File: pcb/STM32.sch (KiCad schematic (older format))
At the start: 30 parts, among them J1 Conn_02x07_Odd_Even, X1 ABM8G

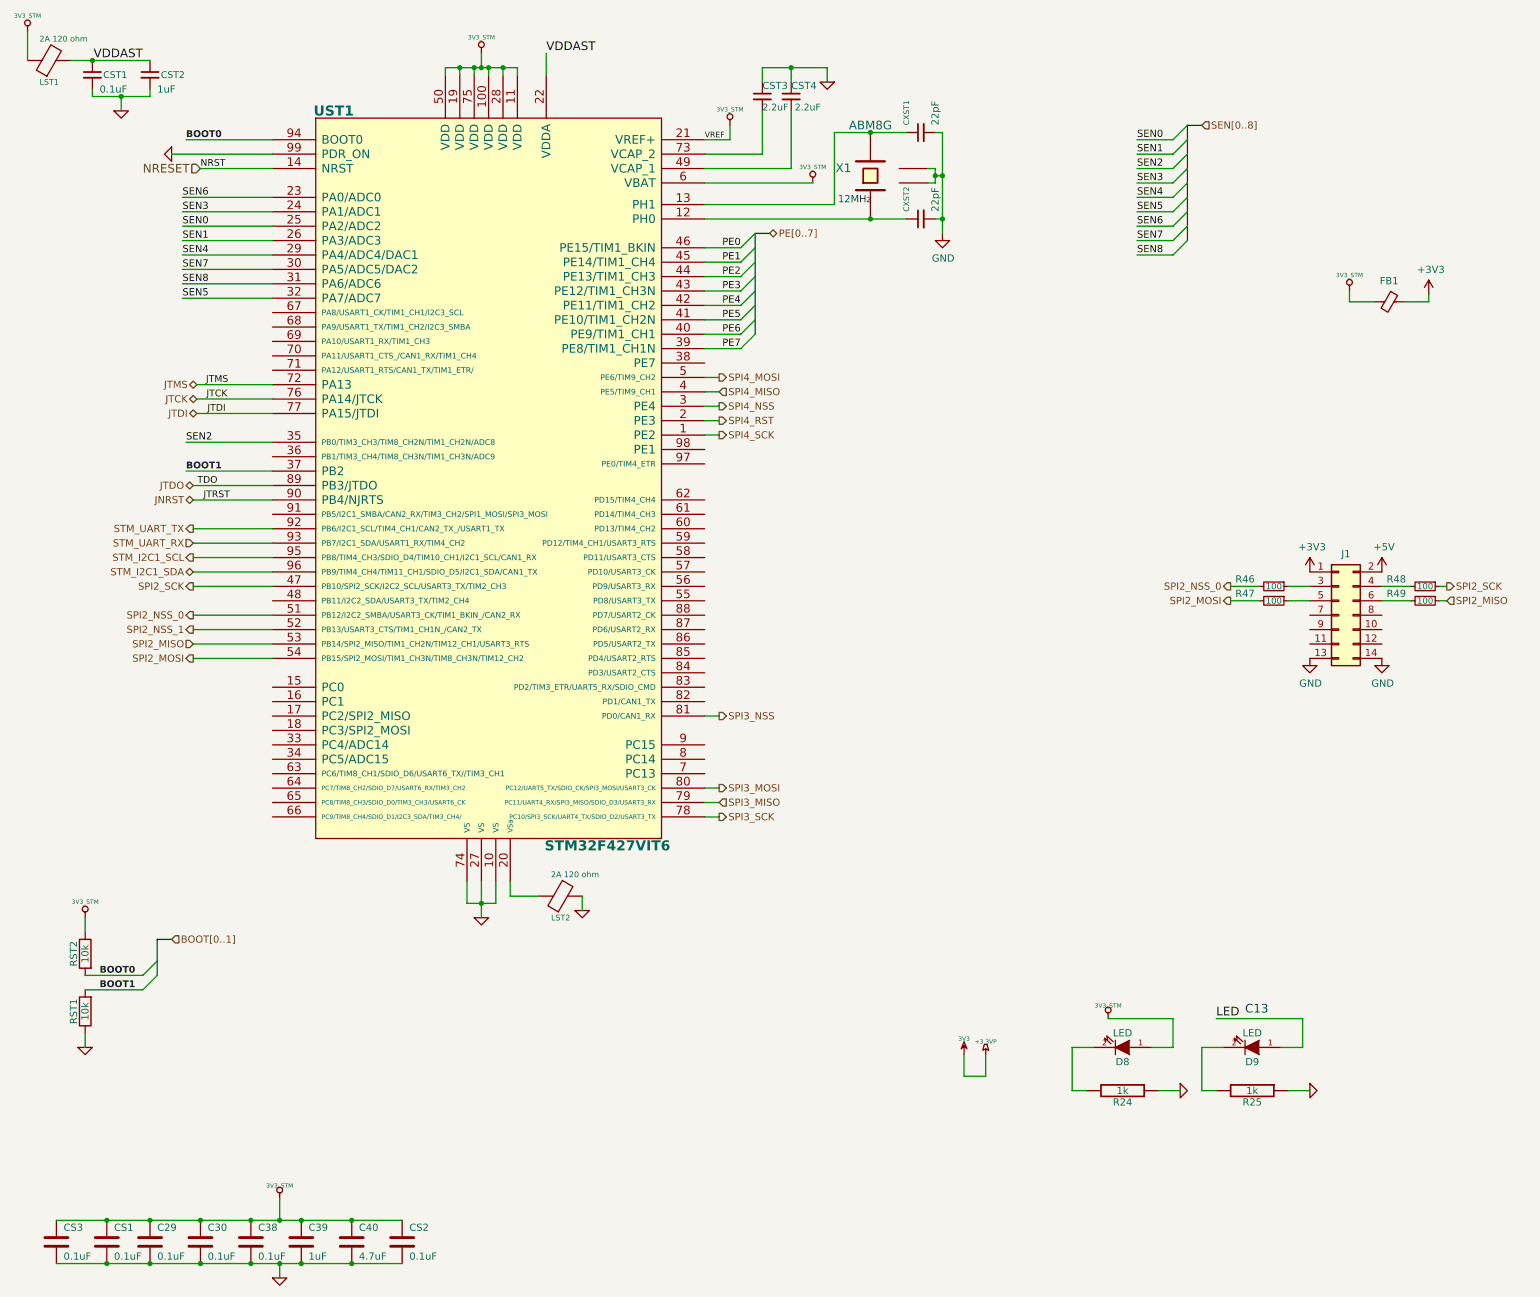
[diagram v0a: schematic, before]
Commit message: recomendations from Carlos Camargo applied
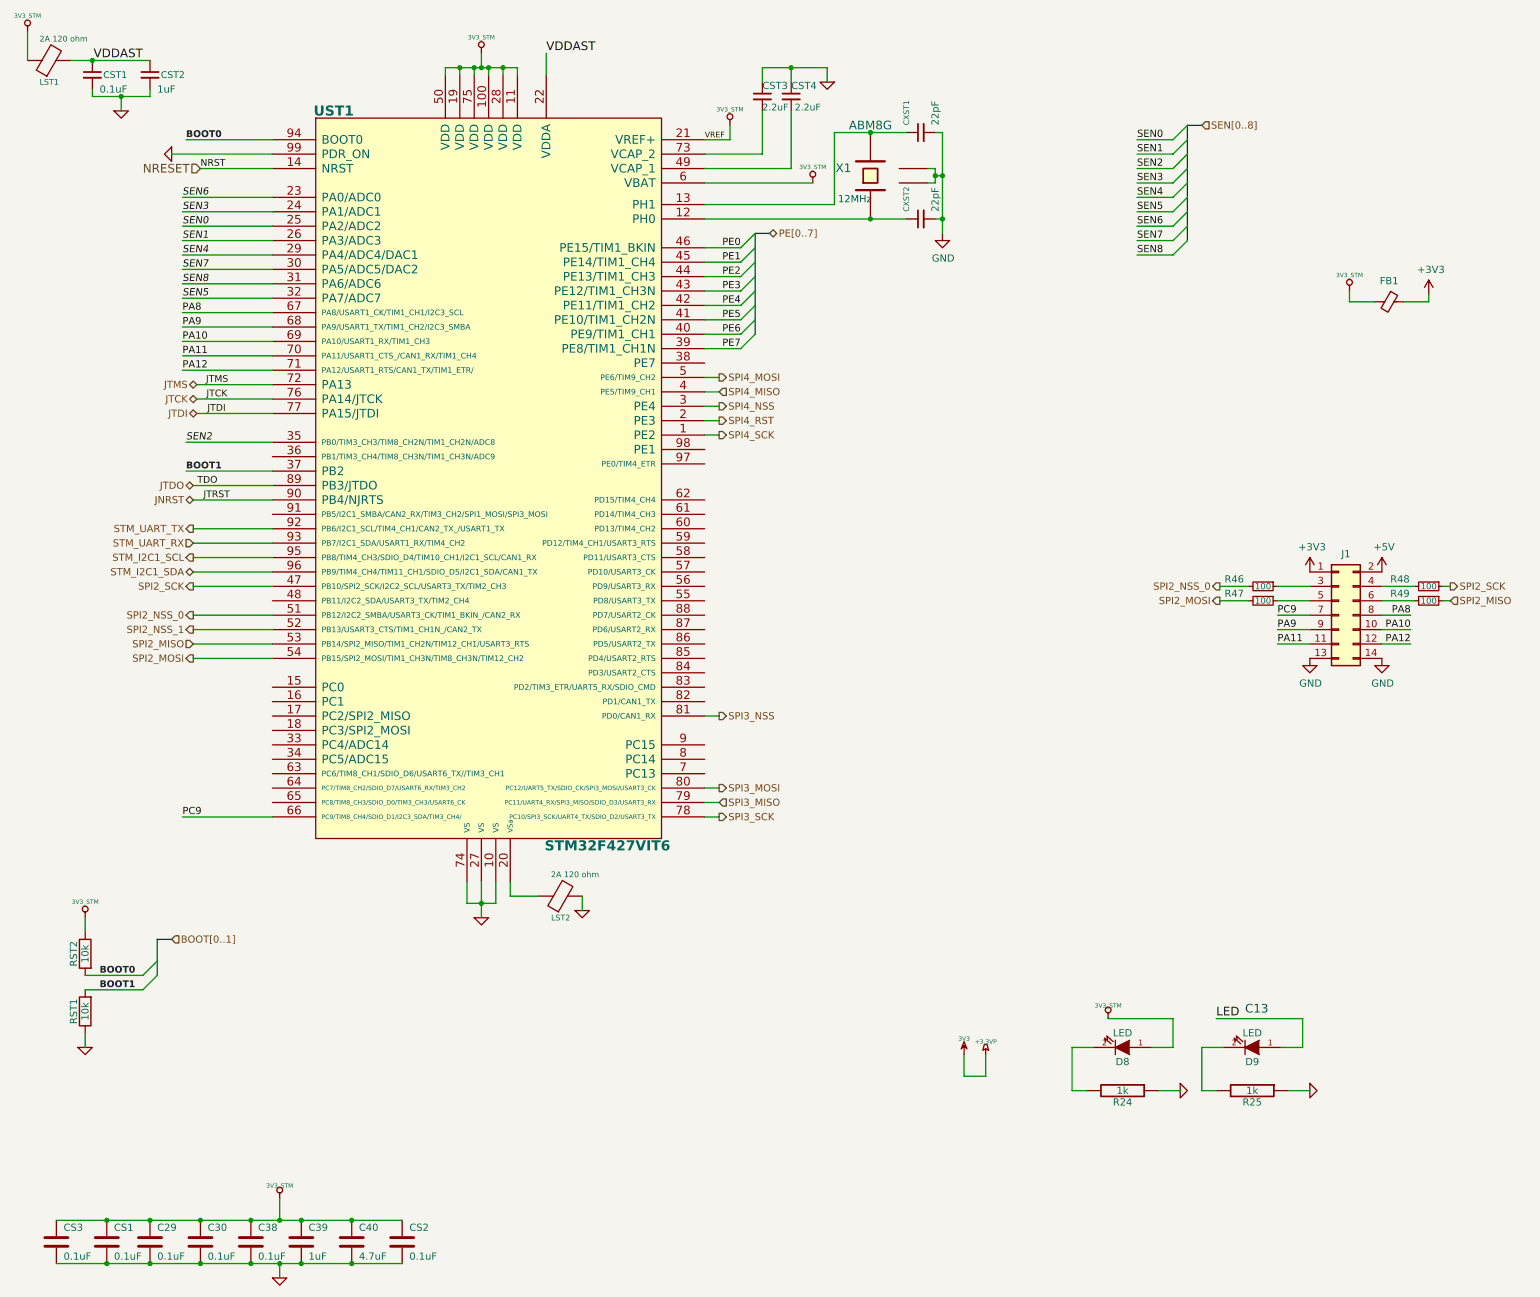
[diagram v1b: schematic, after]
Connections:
- net PC9: now reaches UST1.66 (PC9/TIM8_CH4/SDIO_D1/I2C3_SDA/TIM3_CH4/)
- net PC9: now also J1.7 (Pin_7)
- net PA8: now reaches UST1.67 (PA8/USART1_CK/TIM1_CH1/I2C3_SCL)
- net PA8: now also J1.8 (Pin_8)
- net PA9: now reaches UST1.68 (PA9/USART1_TX/TIM1_CH2/I2C3_SMBA)
- net PA9: now also J1.9 (Pin_9)
- net PA10: now reaches UST1.69 (PA10/USART1_RX/TIM1_CH3)
- net PA10: now also J1.10 (Pin_10)
- net PA11: now reaches UST1.70 (PA11/USART1_CTS_/CAN1_RX/TIM1_CH4)
- net PA11: now also J1.11 (Pin_11)
- net PA12: now reaches UST1.71 (PA12/USART1_RTS/CAN1_TX/TIM1_ETR/)
- net PA12: now also J1.12 (Pin_12)
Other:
- moved on the sheet: R46, R47, R48, R49
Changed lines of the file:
@@
 Text HLabel 2100 1600 0    60   Input ~ 0
 NRESET
-Text Label 1975 1800 0    50   ~ 0
+Text Label 1975 1800 0    50   Italic 0
 SEN6
-Text Label 1975 2500 0    50   ~ 0
+Text Label 1975 2500 0    50   Italic 0
 SEN5
-Text Label 1975 2200 0    50   ~ 0
+Text Label 1975 2200 0    50   Italic 0
 SEN4
-Text Label 1975 1900 0    50   ~ 0
+Text Label 1975 1900 0    50   Italic 0
 SEN3
-Text Label 2000 3500 0    50   ~ 0
+Text Label 2000 3500 0    50   Italic 0
 SEN2
-Text Label 1975 2100 0    50   ~ 0
+Text Label 1975 2100 0    50   Italic 0
 SEN1
 Text Label 2304 3900 2    47   ~ 0
@@
 Text Label 2000 3700 0    47   ~ 9
 BOOT1
-Text Label 1975 2000 0    50   ~ 0
+Text Label 1975 2000 0    50   Italic 0
 SEN0
 $Comp
@@
 Text HLabel 6050 2050 2    50   BiDi ~ 0
 PE[0..7]
-Text Label 1975 2400 0    50   ~ 0
+Text Label 1975 2400 0    50   Italic 0
 SEN8
-Text Label 1975 2300 0    50   ~ 0
+Text Label 1975 2300 0    50   Italic 0
 SEN7
 Text Label 8600 2000 0    50   ~ 0
@@
 Wire Wire Line
 	1300 7300 1700 7300
-Text HLabel 10750 4600 2    50   Input ~ 0
+Text HLabel 10775 4600 2    50   Input ~ 0
 SPI2_MISO
-Text HLabel 9250 4600 0    50   Output ~ 0
+Text HLabel 9175 4600 0    50   Output ~ 0
 SPI2_MOSI
-Text HLabel 9250 4500 0    50   Output ~ 0
+Text HLabel 9175 4500 0    50   Output ~ 0
 SPI2_NSS_0
-Text HLabel 10750 4500 2    50   Output ~ 0
+Text HLabel 10775 4500 2    50   Output ~ 0
 SPI2_SCK
 $Comp
@@
 L Device:R_Small R?
 U 1 1 5EDA5903
-P 9550 4600
+P 9475 4600
 AR Path="/5E96F696/5EDA5903" Ref="R?"  Part="1"
 AR Path="/5E989259/5EDA5903" Ref="R47"  Part="1"
-F 0 "R47" V 9500 4400 50  0000 C CNN
-F 1 "100" V 9550 4600 43  0000 C CNN
-F 2 "Resistor_SMD:R_0402_1005Metric" V 9480 4600 50  0001 C CNN
-F 3 "~" H 9550 4600 50  0001 C CNN
-	1    9550 4600
+F 0 "R47" V 9425 4400 50  0000 C CNN
+F 1 "100" V 9475 4600 43  0000 C CNN
+F 2 "Resistor_SMD:R_0402_1005Metric" V 9405 4600 50  0001 C CNN
+F 3 "~" H 9475 4600 50  0001 C CNN
+	1    9475 4600
 	0    1    1    0
 $EndComp
@@
 L Device:R_Small R?
 U 1 1 5EDD3281
-P 9550 4500
+P 9475 4500
 AR Path="/5E96F696/5EDD3281" Ref="R?"  Part="1"
 AR Path="/5E989259/5EDD3281" Ref="R46"  Part="1"
-F 0 "R46" V 9500 4300 50  0000 C CNN
-F 1 "100" V 9550 4500 43  0000 C CNN
-F 2 "Resistor_SMD:R_0402_1005Metric" V 9480 4500 50  0001 C CNN
-F 3 "~" H 9550 4500 50  0001 C CNN
-	1    9550 4500
+F 0 "R46" V 9425 4300 50  0000 C CNN
+F 1 "100" V 9475 4500 43  0000 C CNN
+F 2 "Resistor_SMD:R_0402_1005Metric" V 9405 4500 50  0001 C CNN
+F 3 "~" H 9475 4500 50  0001 C CNN
+	1    9475 4500
 	0    1    1    0
 $EndComp
 Wire Wire Line
-	9250 4500 9450 4500
-Wire Wire Line
-	9250 4600 9450 4600
-Wire Wire Line
-	9650 4500 9800 4500
-Wire Wire Line
-	9800 4600 9650 4600
+	9175 4500 9375 4500
+Wire Wire Line
+	9175 4600 9375 4600
+Wire Wire Line
+	9575 4500 9800 4500
+Wire Wire Line
+	9800 4600 9575 4600
 $Comp
 L Device:R_Small R?
 U 1 1 5EE12EAD
-P 10600 4600
+P 10625 4600
 AR Path="/5E96F696/5EE12EAD" Ref="R?"  Part="1"
 AR Path="/5E989259/5EE12EAD" Ref="R49"  Part="1"
-F 0 "R49" V 10550 4400 50  0000 C CNN
-F 1 "100" V 10600 4600 43  0000 C CNN
-F 2 "Resistor_SMD:R_0402_1005Metric" V 10530 4600 50  0001 C CNN
-F 3 "~" H 10600 4600 50  0001 C CNN
-	1    10600 4600
+F 0 "R49" V 10575 4400 50  0000 C CNN
+F 1 "100" V 10625 4600 43  0000 C CNN
+F 2 "Resistor_SMD:R_0402_1005Metric" V 10555 4600 50  0001 C CNN
+F 3 "~" H 10625 4600 50  0001 C CNN
+	1    10625 4600
 	0    1    1    0
 $EndComp
@@
 L Device:R_Small R?
 U 1 1 5EE12EB7
-P 10600 4500
+P 10625 4500
 AR Path="/5E96F696/5EE12EB7" Ref="R?"  Part="1"
 AR Path="/5E989259/5EE12EB7" Ref="R48"  Part="1"
-F 0 "R48" V 10550 4300 50  0000 C CNN
-F 1 "100" V 10600 4500 43  0000 C CNN
-F 2 "Resistor_SMD:R_0402_1005Metric" V 10530 4500 50  0001 C CNN
-F 3 "~" H 10600 4500 50  0001 C CNN
-	1    10600 4500
+F 0 "R48" V 10575 4300 50  0000 C CNN
+F 1 "100" V 10625 4500 43  0000 C CNN
+F 2 "Resistor_SMD:R_0402_1005Metric" V 10555 4500 50  0001 C CNN
+F 3 "~" H 10625 4500 50  0001 C CNN
+	1    10625 4500
 	0    1    1    0
 $EndComp
 Wire Wire Line
-	10300 4500 10500 4500
-Wire Wire Line
-	10300 4600 10500 4600
-Wire Wire Line
-	10750 4500 10700 4500
-Wire Wire Line
-	10750 4600 10700 4600
+	10300 4500 10525 4500
+Wire Wire Line
+	10300 4600 10525 4600
+Wire Wire Line
+	10775 4500 10725 4500
+Wire Wire Line
+	10775 4600 10725 4600
+Text Label 10500 4800 2    50   ~ 0
+PA10
+Text Label 10500 4900 2    50   ~ 0
+PA12
+Text Label 10500 4700 2    50   ~ 0
+PA8
+Wire Wire Line
+	10500 4700 10300 4700
+Wire Wire Line
+	10500 4900 10300 4900
+Wire Wire Line
+	10500 4800 10300 4800
+Wire Wire Line
+	9575 4700 9800 4700
+Wire Wire Line
+	9575 4900 9800 4900
+Wire Wire Line
+	9575 4800 9800 4800
+Text Label 9575 4800 0    50   ~ 0
+PA9
+Text Label 9575 4900 0    50   ~ 0
+PA11
+Wire Wire Line
+	1975 3000 2600 3000
+Text Label 1975 3000 0    50   ~ 0
+PA12
+Wire Wire Line
+	1975 2900 2600 2900
+Wire Wire Line
+	1975 2800 2600 2800
+Wire Wire Line
+	1975 2700 2600 2700
+Wire Wire Line
+	1975 2600 2600 2600
+Text Label 1975 2700 0    50   ~ 0
+PA9
+Text Label 1975 2800 0    50   ~ 0
+PA10
+Text Label 1975 2600 0    50   ~ 0
+PA8
+Text Label 1975 2900 0    50   ~ 0
+PA11
+Wire Wire Line
+	1975 6100 2600 6100
+Text Label 1975 6100 0    50   ~ 0
+PC9
+Text Label 9575 4700 0    50   ~ 0
+PC9
 Wire Bus Line
 	1800 6950 1800 7200

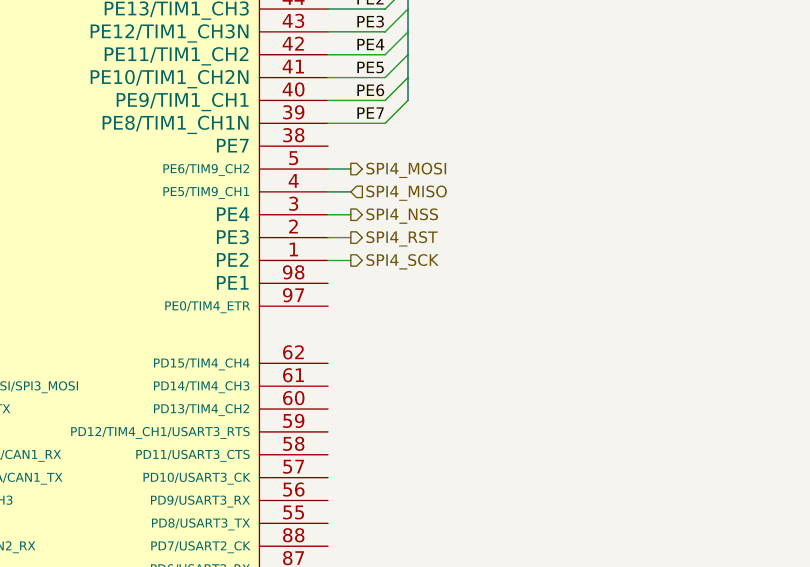
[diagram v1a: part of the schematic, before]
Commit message: 2 CS for FPGA
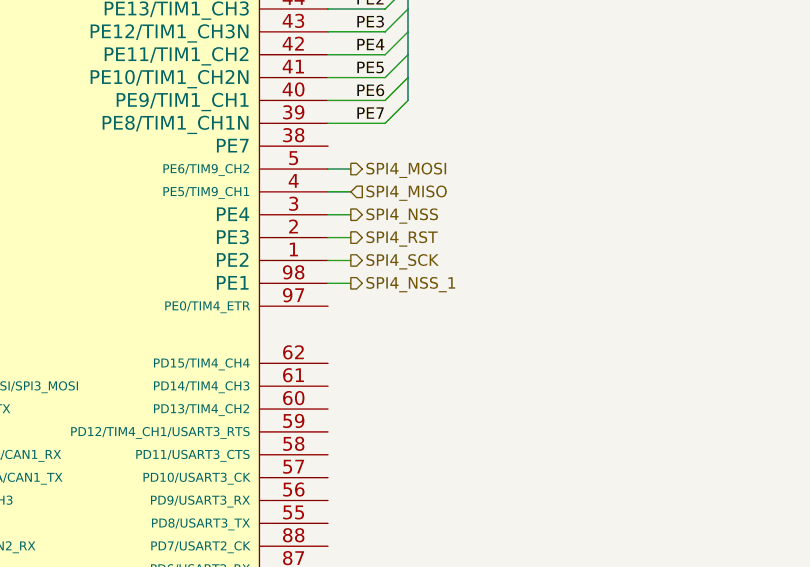
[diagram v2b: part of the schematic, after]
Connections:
- net SPI4_NSS_1: now reaches UST1.98 (PE1)
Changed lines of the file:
@@
 Text Label 9575 4700 0    50   ~ 0
 PC9
+Text HLabel 5700 3550 2    50   Output ~ 0
+SPI4_NSS_1
+Wire Wire Line
+	5700 3550 5600 3550
 Wire Bus Line
 	1800 6950 1800 7200

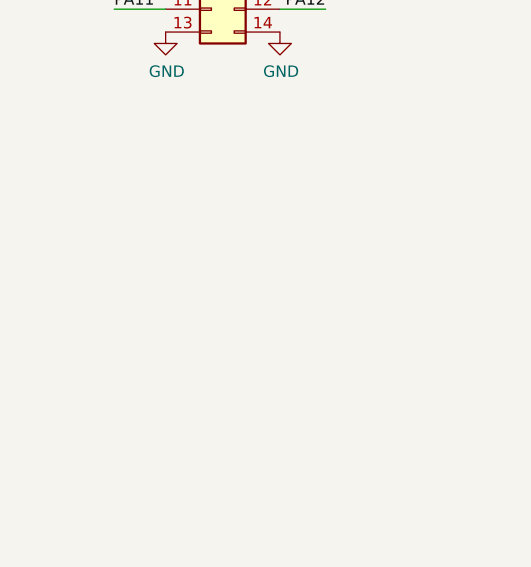
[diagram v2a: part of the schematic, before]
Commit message: improving ground separation
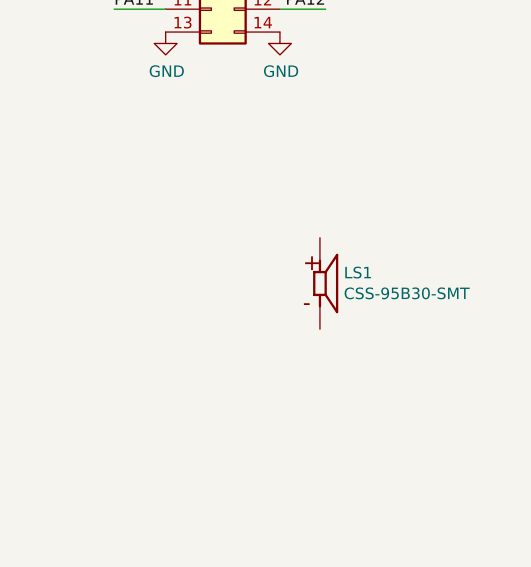
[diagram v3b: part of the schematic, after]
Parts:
- added LS1: CSS-95B30-SMT, SMD:CUI_CSS-95B30-SMT, symbol CSS-95B30-SMT:CSS-95B30-SMT
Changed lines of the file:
@@
 Wire Bus Line
 	8950 1300 8950 2100
+$Comp
+L CSS-95B30-SMT:CSS-95B30-SMT LS1
+U 1 1 5EBB81C9
+P 10475 6100
+F 0 "LS1" H 10579 6146 50  0000 L CNN
+F 1 "CSS-95B30-SMT" H 10579 6055 50  0000 L CNN
+F 2 "SMD:CUI_CSS-95B30-SMT" H 10475 6100 50  0001 L BNN
+F 3 "CSS-95B30-SMT" H 10475 6100 50  0001 L BNN
+F 4 "None" H 10475 6100 50  0001 L BNN "Field4"
+F 5 "CUI" H 10475 6100 50  0001 L BNN "Field5"
+F 6 "None" H 10475 6100 50  0001 L BNN "Field6"
+F 7 "Unavailable" H 10475 6100 50  0001 L BNN "Field7"
+F 8 "10 mm, 5 V, 92 dB, Surface Mount _SMT_, Magnetic Audio Transducer Buzzer" H 10475 6100 50  0001 L BNN "Field8"
+	1    10475 6100
+	1    0    0    -1
+$EndComp
 $EndSCHEMATC
